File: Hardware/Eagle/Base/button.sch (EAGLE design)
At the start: 11 parts, among them SW2 SPST_TACT-EVQQ2, X1 1365-10

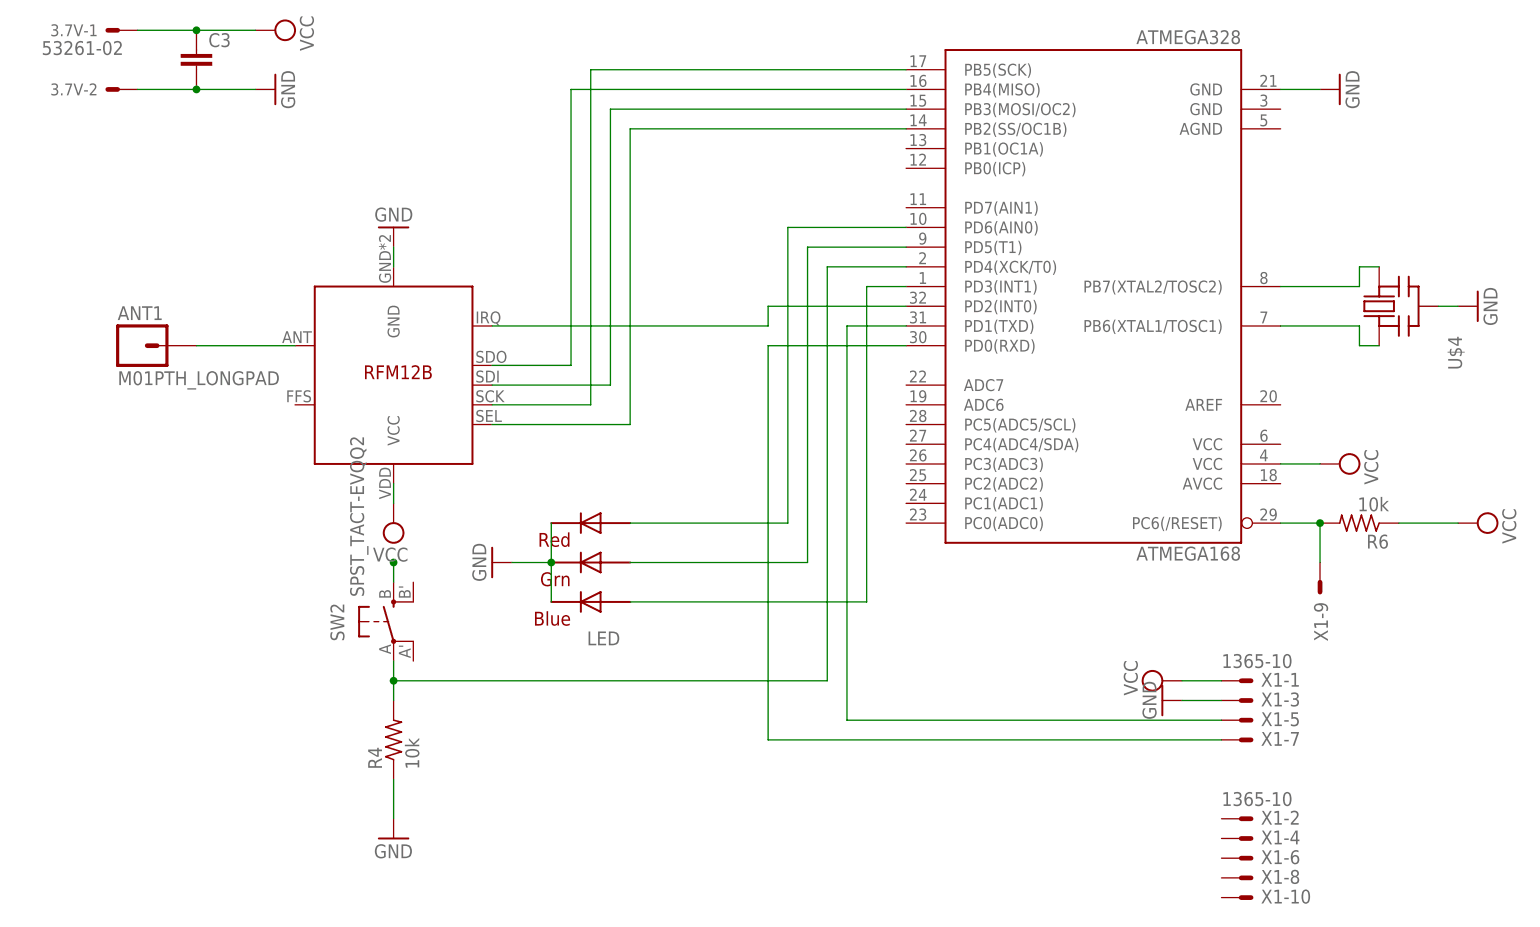
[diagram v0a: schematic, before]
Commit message: Button hardware changes
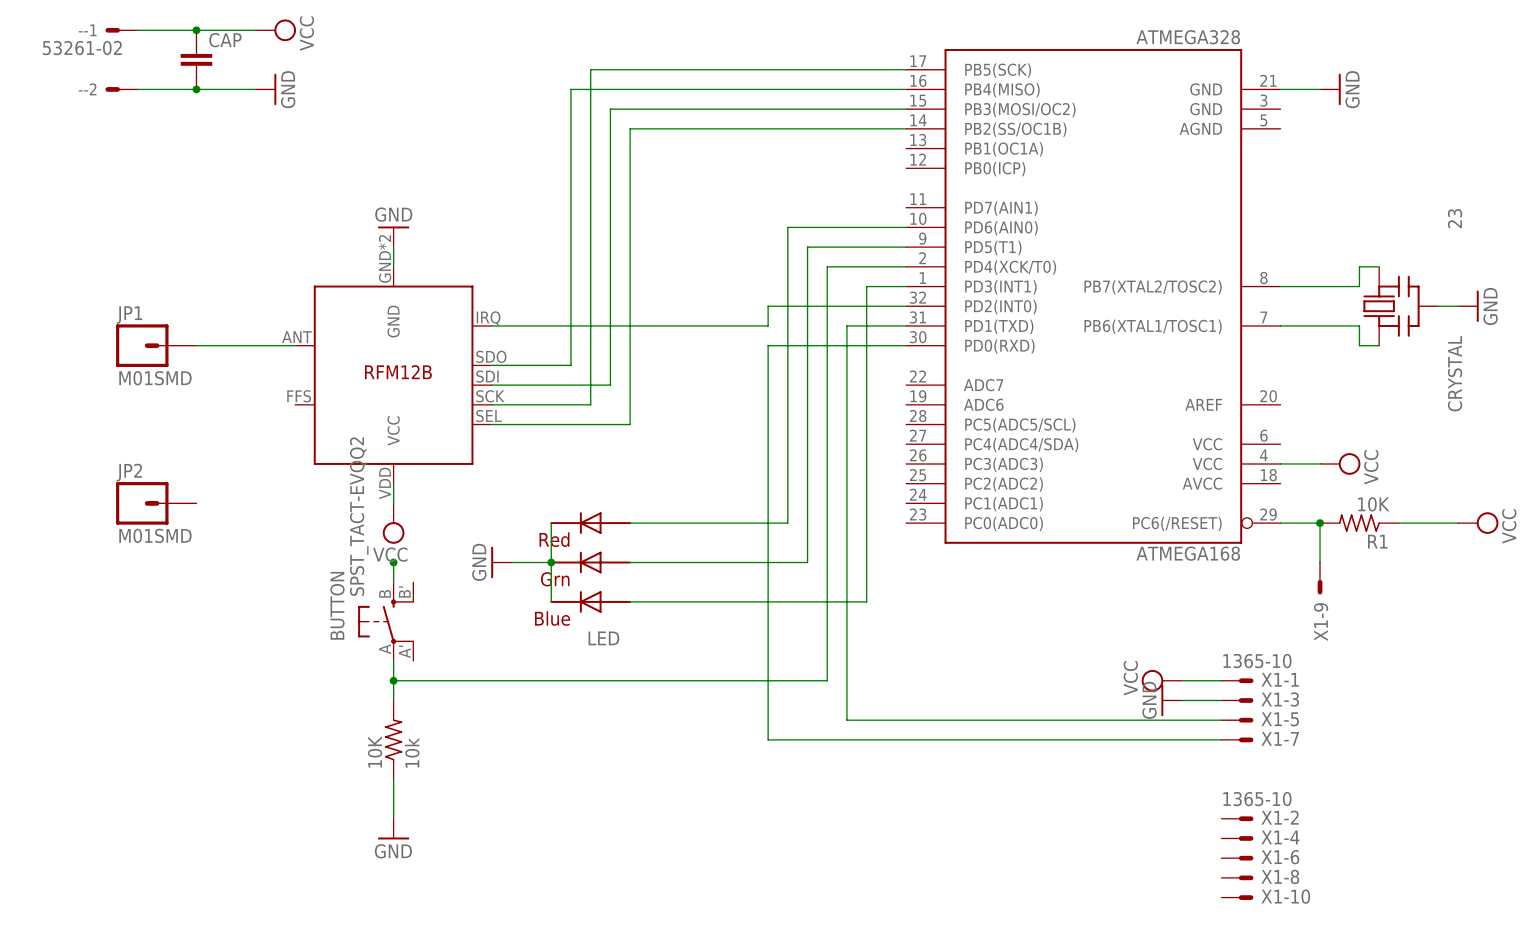
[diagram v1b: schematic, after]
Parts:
- removed ANT1: M01PTH_LONGPAD, SparkFun:M01PTH_LONGPAD
- added JP1, JP2: M01SMD, SparkFun:M01SMD
- CRYSTAL: value (none) -> 23
- R1: value 10k -> 10K
- RFM12B: value RFM12BRMF12BGND -> RFM12B
- renumbered 3.7V to -, C3 to CAP, R4 to 10K, R6 to R1, SW2 to BUTTON, U$2 to RFM12B, U$4 to CRYSTAL
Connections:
- net N$25: now also JP1.1; no longer ANT1.1
